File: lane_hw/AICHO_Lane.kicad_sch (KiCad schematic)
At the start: 63 parts, among them J1 JST PH, J2 RJ45, J41 JST PH, J42 JST PH, J43 JST PH, J9 Conn_01x04, Q41 AO3400A, Q42 AO3400A, Q43 AO3400A, U1 TPS54302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

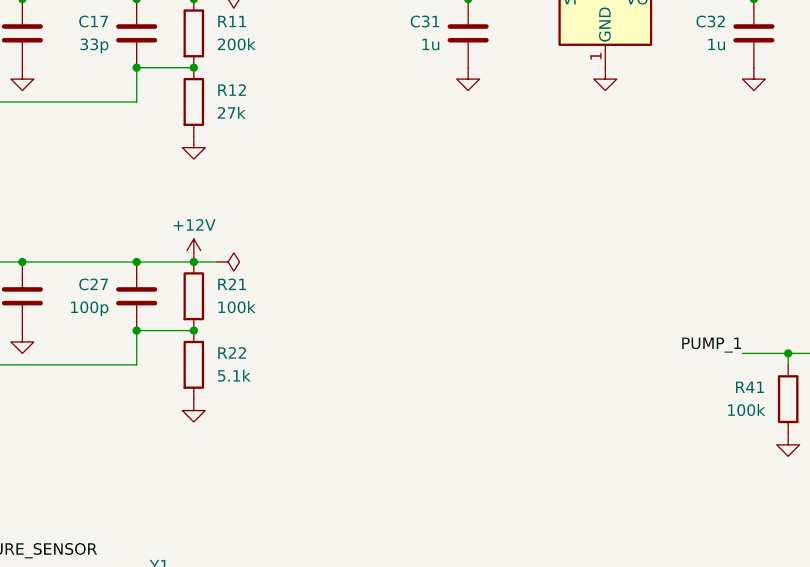
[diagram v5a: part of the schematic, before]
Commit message: lane_hw: Add bulk capacitor at 12-V output
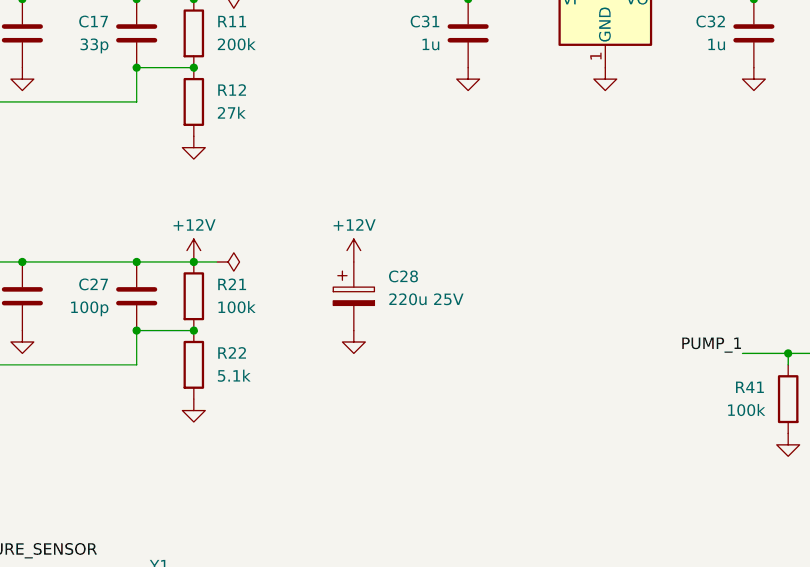
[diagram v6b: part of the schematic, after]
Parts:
- added C28: 220u 25V, Capacitor_SMD:CP_Elec_6.3x7.7, symbol Device:C_Polarized
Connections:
- net +12V: now also C28.1
- net GND: now also C28.2
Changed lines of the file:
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@@
+	)
+	(symbol
+		(lib_id "power:GND")
+		(at 168.91 68.58 0)
+		(unit 1)
+		(exclude_from_sim no)
+		(in_bom yes)
+		(on_board yes)
+		(dnp no)
+		(fields_autoplaced yes)
+		(property "Reference" "#PWR072"
+			(at 168.91 74.93 0)
+			(effects
+				(font
+					(size 1.27 1.27)
+				)
+				(hide yes)
+			)
+		)
+		(property "Value" "GND"
+			(at 168.91 73.66 0)
+			(effects
+				(font
+					(size 1.27 1.27)
+				)
+				(hide yes)
+			)
+		)
+		(property "Footprint" ""
+			(at 168.91 68.58 0)
+			(effects
+				(font
+					(size 1.27 1.27)
+				)
+				(hide yes)
+			)
+		)
+		(property "Datasheet" ""
+			(at 168.91 68.58 0)
+			(effects
+				(font
+					(size 1.27 1.27)
+				)
+				(hide yes)
+			)
+		)
+		(property "Description" "Power symbol creates a global label with name \"GND\" , ground"
+			(at 168.91 68.58 0)
+			(effects
+				(font
+					(size 1.27 1.27)
+				)
+				(hide yes)
+			)
+		)
+		(pin "1"
+		)
+		(instances
+			(project "AICHO_Lane"
+				(path "/6c51c4e7-714d-4ba2-b183-a9bbda12c420"
+					(reference "#PWR072")
+					(unit 1)
+				)
+			)
+		)
+	)
+	(symbol
+		(lib_id "Device:C_Polarized")
+		(at 168.91 64.77 0)
+		(unit 1)
+		(exclude_from_sim no)
+		(in_bom yes)
+		(on_board yes)
+		(dnp no)
+		(fields_autoplaced yes)
+		(property "Reference" "C28"
+			(at 172.72 62.6109 0)
+			(effects
+				(font
+					(size 1.27 1.27)
+				)
+				(justify left)
+			)
+		)
+		(property "Value" "220u 25V"
+			(at 172.72 65.1509 0)
+			(effects
+				(font
+					(size 1.27 1.27)
+				)
+				(justify left)
+			)
+		)
+		(property "Footprint" "Capacitor_SMD:CP_Elec_6.3x7.7"
+			(at 169.8752 68.58 0)
+			(effects
+				(font
+					(size 1.27 1.27)
+				)
+				(hide yes)
+			)
+		)
+		(property "Datasheet" "~"
+			(at 168.91 64.77 0)
+			(effects
+				(font
+					(size 1.27 1.27)
+				)
+				(hide yes)
+			)
+		)
+		(property "Description" "Polarized capacitor"
+			(at 168.91 64.77 0)
+			(effects
+				(font
+					(size 1.27 1.27)
+				)
+				(hide yes)
+			)
+		)
+		(property "LCSC PN" "C696188"
+			(at 168.91 64.77 0)
+			(effects
+				(font
+					(size 1.27 1.27)
+				)
+				(hide yes)
+			)
+		)
+		(property "Mfr PN" "RVT1E221M0607"
+			(at 168.91 64.77 0)
+			(effects
+				(font
+					(size 1.27 1.27)
+				)
+				(hide yes)
+			)
+		)
+		(pin "1"
+		)
+		(pin "2"
+		)
+		(instances
+			(project ""
+				(path "/6c51c4e7-714d-4ba2-b183-a9bbda12c420"
+					(reference "C28")
+					(unit 1)
+				)
+			)
+		)
 	)
 	(symbol
@@
 					(unit 1)
 				)
+			)
+		)
+	)
+	(symbol
+		(lib_id "power:+12V")
+		(at 168.91 60.96 0)
+		(unit 1)
+		(exclude_from_sim no)
+		(in_bom yes)
+		(on_board yes)
+		(dnp no)
+		(property "Reference" "#PWR071"
+			(at 168.91 64.77 0)
+			(effects
+				(font
+					(size 1.27 1.27)
+				)
+				(hide yes)
+			)
+		)
+		(property "Value" "+12V"
+			(at 168.91 56.896 0)
+			(effects
+				(font
+					(size 1.27 1.27)
+				)
+			)
+		)
+		(property "Footprint" ""
+			(at 168.91 60.96 0)
+			(effects
+				(font
+					(size 1.27 1.27)
+				)
+				(hide yes)
+			)
+		)
+		(property "Datasheet" ""
+			(at 168.91 60.96 0)
+			(effects
+				(font
+					(size 1.27 1.27)
+				)
+				(hide yes)
+			)
+		)
+		(property "Description" "Power symbol creates a global label with name \"+12V\""
+			(at 168.91 60.96 0)
+			(effects
+				(font
+					(size 1.27 1.27)
+				)
+				(hide yes)
+			)
+		)
+		(pin "1"
+		)
+		(instances
+			(project "AICHO_Lane"
+				(path "/6c51c4e7-714d-4ba2-b183-a9bbda12c420"
+					(reference "#PWR071")
+					(unit 1)
+				)

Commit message: lane_hw: Further layout
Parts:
- added C5: 100n, Capacitor_SMD:C_0402_1005Metric, symbol Device:C
- C4: value 100n -> 1u
- renumbered C5 to C6, C6 to C7
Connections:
- net +5V: now also C5.2
- net ACT_LED: now also U4.16 (PA0); no longer U4.11 (PB7)
- net GND: now also C5.1
- net PRESSURE_SENSOR: now also U4.3 (PA7); no longer U4.16 (PA0)
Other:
- moved on the sheet: C4
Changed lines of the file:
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@@
 	)
 	(junction
-		(at 237.49 101.6)
+		(at 88.9 144.78)
 		(diameter 0)
 		(color 0 0 0 0)
 	)
 	(junction
-		(at 116.84 154.94)
+		(at 237.49 101.6)
 		(diameter 0)
 		(color 0 0 0 0)
 	)
 	(junction
-		(at 100.33 147.32)
+		(at 116.84 154.94)
 		(diameter 0)
 		(color 0 0 0 0)
@@
 	)
 	(junction
+		(at 100.33 144.78)
+		(diameter 0)
+		(color 0 0 0 0)
+	)
+	(junction
 		(at 181.61 31.75)
 		(diameter 0)
@@
 	)
 	(no_connect
+		(at 132.08 113.03)
+	)
+	(no_connect
 		(at 120.65 121.92)
 	)
@@
 		(at 152.4 143.51)
 	)
-	(no_connect
-		(at 104.14 107.95)
+	(wire
+		(pts
+			(xy 100.33 143.51) (xy 100.33 144.78)
+		)
+		(stroke
+			(width 0)
+			(type default)
+		)
 	)
 	(wire
 		(pts
-			(xy 100.33 143.51) (xy 100.33 147.32)
+			(xy 88.9 144.78) (xy 100.33 144.78)
 		)
 		(stroke
@@
 	(wire
 		(pts
+			(xy 86.36 151.13) (xy 88.9 151.13)
+		)
+		(stroke
+			(width 0)
+			(type default)
+		)
+	)
+	(wire
+		(pts
 			(xy 144.78 39.37) (xy 151.13 39.37)
 		)
@@
 	(wire
 		(pts
+			(xy 88.9 151.13) (xy 88.9 144.78)
+		)
+		(stroke
+			(width 0)
+			(type default)
+		)
+	)
+	(wire
+		(pts
 			(xy 144.78 31.75) (xy 151.13 31.75)
 		)
@@
 	(wire
 		(pts
-			(xy 100.33 147.32) (xy 100.33 148.59)
-		)
-		(stroke
-			(width 0)
-			(type default)
-		)
-	)
-	(wire
-		(pts
 			(xy 237.49 80.01) (xy 237.49 76.2)
 		)
@@
 	(wire
 		(pts
+			(xy 100.33 144.78) (xy 100.33 148.59)
+		)
+		(stroke
+			(width 0)
+			(type default)
+		)
+	)
+	(wire
+		(pts
 			(xy 237.49 93.98) (xy 237.49 96.52)
 		)
@@
 	(wire
 		(pts
+			(xy 74.93 151.13) (xy 78.74 151.13)
+		)
+		(stroke
+			(width 0)
+			(type default)
+		)
+	)
+	(wire
+		(pts
 			(xy 90.17 161.29) (xy 90.17 163.83)
 		)
@@
 	(wire
 		(pts
-			(xy 83.82 147.32) (xy 87.63 147.32)
+			(xy 74.93 144.78) (xy 78.74 144.78)
 		)
 		(stroke
@@
 	(wire
 		(pts
-			(xy 95.25 147.32) (xy 100.33 147.32)
+			(xy 86.36 144.78) (xy 88.9 144.78)
 		)
 		(stroke
@@
 	)
 	(label "ACT_LED"
-		(at 132.08 113.03 0)
+		(at 123.19 93.98 0)
 		(effects
 			(font
@@
 	)
 	(label "PRESSURE_SENSOR"
-		(at 123.19 93.98 0)
+		(at 104.14 107.95 180)
 		(effects
 			(font
 				(size 1.27 1.27)
 			)
-			(justify left bottom)
+			(justify right bottom)
 		)
 	)
@@
 		(on_board yes)
 		(dnp no)
-		(property "Reference" "C6"
+		(property "Reference" "C7"
 			(at 167.386 158.75 0)
 			(effects
@@
 			(project "AICHO_Lane"
 				(path "/6c51c4e7-714d-4ba2-b183-a9bbda12c420"
-					(reference "C6")
+					(reference "C7")
 					(unit 1)
 				)
@@
 	(symbol
 		(lib_id "Device:C")
-		(at 91.44 147.32 90)
+		(at 82.55 144.78 90)
 		(unit 1)
 		(exclude_from_sim no)
@@
 		(dnp no)
 		(property "Reference" "C4"
-			(at 88.646 143.256 90)
+			(at 79.756 140.716 90)
 			(effects
 				(font
@@
 			)
 		)
-		(property "Value" "100n"
-			(at 93.98 143.256 90)
+		(property "Value" "1u"
+			(at 85.09 140.716 90)
 			(effects
 				(font
@@
 		)
 		(property "Footprint" "Capacitor_SMD:C_0402_1005Metric"
-			(at 95.25 146.3548 0)
+			(at 86.36 143.8148 0)
 			(effects
 				(font
@@
 		)
 		(property "Datasheet" "~"
-			(at 91.44 147.32 0)
+			(at 82.55 144.78 0)
 			(effects
 				(font
@@
 		)
 		(property "Description" "Unpolarized capacitor"
-			(at 91.44 147.32 0)
+			(at 82.55 144.78 0)
 			(effects
 				(font
@@
 	)
 	(symbol
+		(lib_id "power:GND")
+		(at 74.93 151.13 0)
+		(unit 1)
+		(exclude_from_sim no)
+		(in_bom yes)
+		(on_board yes)
+		(dnp no)
+		(fields_autoplaced yes)
+		(property "Reference" "#PWR073"
+			(at 74.93 157.48 0)
+			(effects
+				(font
+					(size 1.27 1.27)
+				)
+				(hide yes)
+			)
+		)
+		(property "Value" "GND"
+			(at 74.93 156.21 0)
+			(effects
+				(font
+					(size 1.27 1.27)
+				)
+				(hide yes)
+			)
+		)
+		(property "Footprint" ""
+			(at 74.93 151.13 0)
+			(effects
+				(font
+					(size 1.27 1.27)
+				)
+				(hide yes)
+			)
+		)
+		(property "Datasheet" ""
+			(at 74.93 151.13 0)
+			(effects
+				(font
+					(size 1.27 1.27)
+				)
+				(hide yes)
+			)
+		)
+		(property "Description" "Power symbol creates a global label with name \"GND\" , ground"
+			(at 74.93 151.13 0)
+			(effects
+				(font
+					(size 1.27 1.27)
+				)
+				(hide yes)
+			)
+		)
+		(pin "1"
+		)
+		(instances
+			(project "AICHO_Lane"
+				(path "/6c51c4e7-714d-4ba2-b183-a9bbda12c420"
+					(reference "#PWR073")
+					(unit 1)
+				)
+			)
+		)
+	)
+	(symbol
 		(lib_id "Device:C")
 		(at 119.38 35.56 0)
@@
 	(symbol
 		(lib_id "power:GND")
-		(at 83.82 147.32 0)
+		(at 74.93 144.78 0)
 		(unit 1)
 		(exclude_from_sim no)
@@
 		(fields_autoplaced yes)
 		(property "Reference" "#PWR036"
-			(at 83.82 153.67 0)
+			(at 74.93 151.13 0)
 			(effects
 				(font
@@
 		)
 		(property "Value" "GND"
-			(at 83.82 152.4 0)
+			(at 74.93 149.86 0)
 			(effects
 				(font
@@
 		)
 		(property "Footprint" ""
-			(at 83.82 147.32 0)
+			(at 74.93 144.78 0)
 			(effects
 				(font
@@
 		)
 		(property "Datasheet" ""
-			(at 83.82 147.32 0)
+			(at 74.93 144.78 0)
 			(effects
 				(font
@@
 		)
 		(property "Description" "Power symbol creates a global label with name \"GND\" , ground"
-			(at 83.82 147.32 0)
+			(at 74.93 144.78 0)
 			(effects
 				(font
@@
 		(on_board yes)
 		(dnp no)
-		(property "Reference" "C5"
+		(property "Reference" "C6"
 			(at 144.526 148.59 0)
 			(effects
@@
 			(project "AICHO_Lane"
 				(path "/6c51c4e7-714d-4ba2-b183-a9bbda12c420"
-					(reference "C5")
+					(reference "C6")
 					(unit 1)
 				)
@@
 					(unit 1)
 				)
+			)
+		)
+	)
+	(symbol
+		(lib_id "Device:C")
+		(at 82.55 151.13 90)
+		(unit 1)
+		(exclude_from_sim no)
+		(in_bom yes)
+		(on_board yes)
+		(dnp no)
+		(property "Reference" "C5"
+			(at 79.756 147.066 90)
+			(effects
+				(font
+					(size 1.27 1.27)
+				)
+			)
+		)
+		(property "Value" "100n"
+			(at 85.09 147.066 90)
+			(effects
+				(font
+					(size 1.27 1.27)
+				)
+			)
+		)
+		(property "Footprint" "Capacitor_SMD:C_0402_1005Metric"
+			(at 86.36 150.1648 0)
+			(effects
+				(font
+					(size 1.27 1.27)
+				)
+				(hide yes)
+			)
+		)
+		(property "Datasheet" "~"
+			(at 82.55 151.13 0)
+			(effects
+				(font
+					(size 1.27 1.27)
+				)
+				(hide yes)
+			)
+		)
+		(property "Description" "Unpolarized capacitor"
+			(at 82.55 151.13 0)
+			(effects
+				(font
+					(size 1.27 1.27)
+				)
+				(hide yes)
+			)
+		)
+		(pin "1"
+		)
+		(pin "2"
+		)
+		(instances
+			(project "AICHO_Lane"
+				(path "/6c51c4e7-714d-4ba2-b183-a9bbda12c420"
+					(reference "C5")
+					(unit 1)
+				)

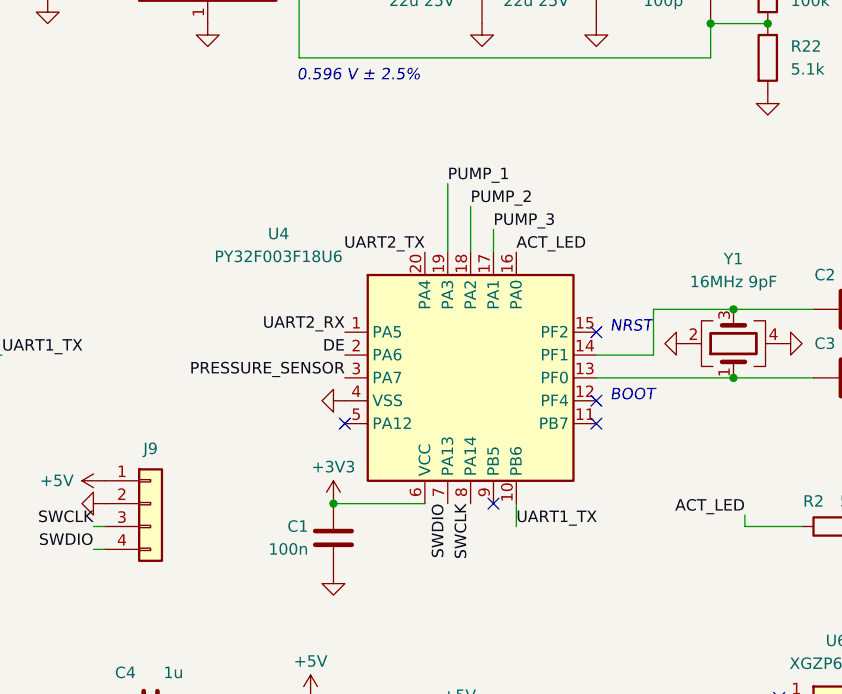
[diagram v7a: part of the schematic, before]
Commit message: lane_hw: Revise board dimensions and layout
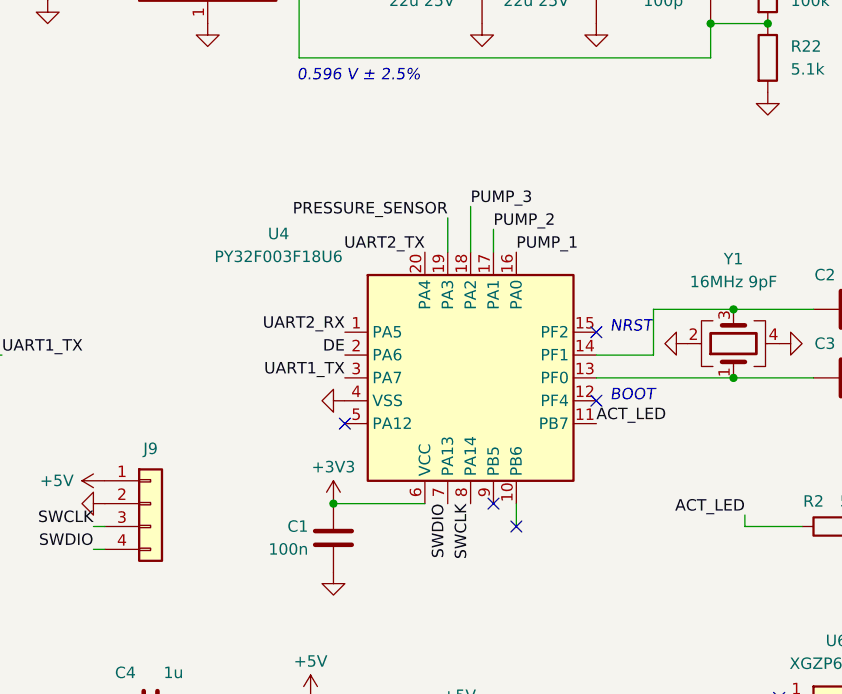
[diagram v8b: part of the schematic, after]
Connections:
- net ACT_LED: now also U4.11 (PB7); no longer U4.16 (PA0)
- net PRESSURE_SENSOR: now also U4.19 (PA3); no longer U4.3 (PA7)
- net PUMP_1: now also U4.16 (PA0); no longer U4.19 (PA3)
- net PUMP_2: now also U4.17 (PA1); no longer U4.18 (PA2)
- net PUMP_3: now also U4.18 (PA2); no longer U4.17 (PA1)
- net UART1_TX: now also U4.3 (PA7); no longer U4.10 (PB6)
